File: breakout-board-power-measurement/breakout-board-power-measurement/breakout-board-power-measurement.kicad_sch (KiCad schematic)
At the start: 83 parts, among them J1 Screw_Terminal_01x04, J2 Conn_01x09, J3 Conn_01x07, J4 Conn_01x02, U1 MCP3911A0-E-SS, U2 Si8641BA-B-IU, U3 LM317_TO-252, Y1 10M

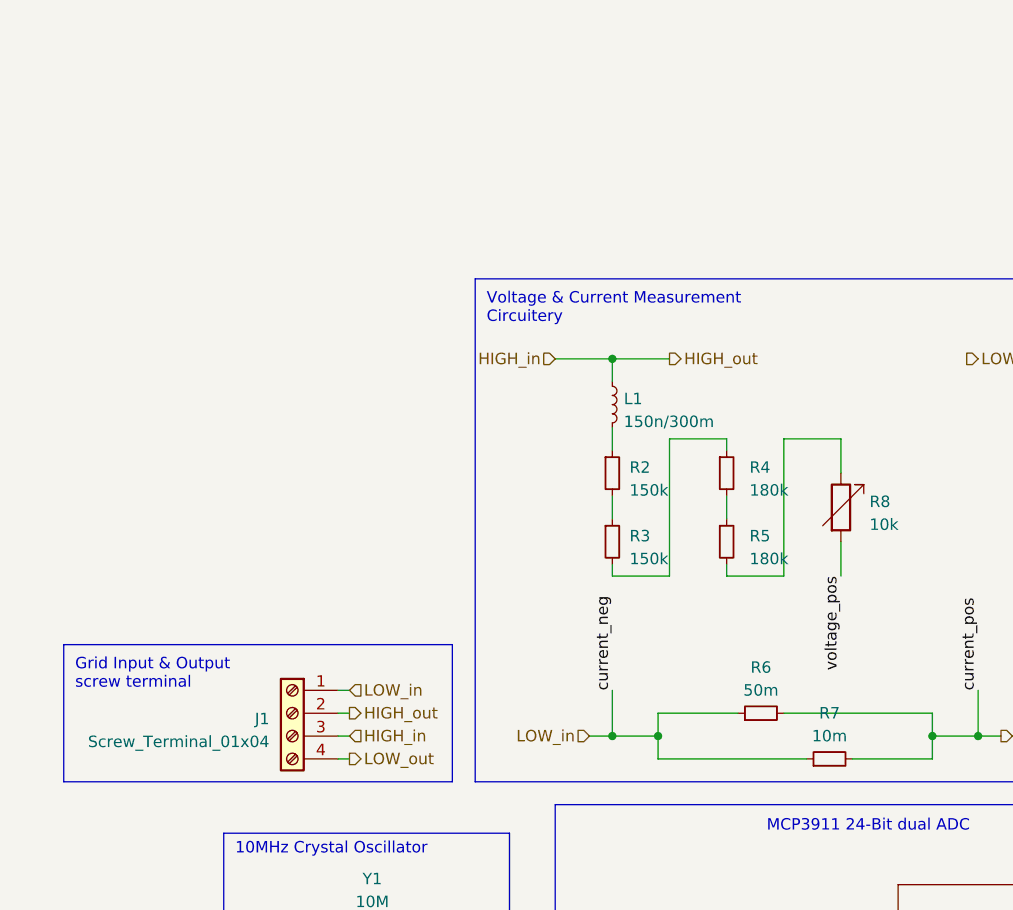
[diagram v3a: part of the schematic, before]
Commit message: Updated PCB layout according to new schematic.(ASM1117-> LM317) (Beidl update)
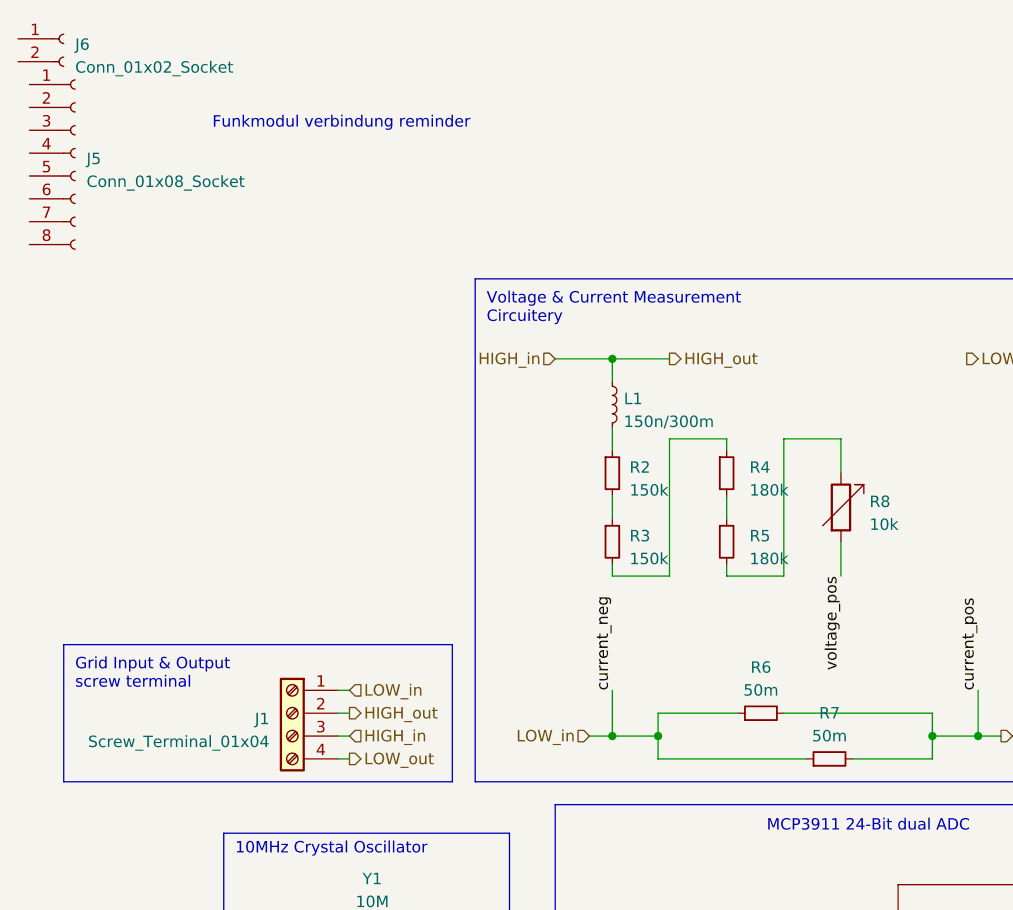
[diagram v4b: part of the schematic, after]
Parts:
- added J5: Conn_01x08_Socket, symbol Connector:Conn_01x08_Socket
- added J6: Conn_01x02_Socket, symbol Connector:Conn_01x02_Socket
- R7: value 10m -> 50m
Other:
- note added: "Funkmodul verbindung reminder"
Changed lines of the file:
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@@
+    (effects (font (size 1.27 1.27)) (justify left bottom))
+  )
+  (text "Funkmodul verbindung reminder\n" (at 44.45 35.56 0)
     (effects (font (size 1.27 1.27)) (justify left bottom))
   )
@@
       (effects (font (size 1.27 1.27)))
     )
-    (property "Value" "10m" (at 113.03 102.87 90)
+    (property "Value" "50m" (at 113.03 102.87 90)
       (effects (font (size 1.27 1.27)))
     )
@@
         (path "/433e477a-c382-4a77-a1aa-b42c4a1fe28b"
           (reference "#PWR011") (unit 1)
+        )
+      )
+    )
+  )
+  (symbol (lib_id "Connector:Conn_01x02_Socket") (at 27.94 25.4 0) (unit 1)
+    (in_bom yes) (on_board yes) (dnp no) (fields_autoplaced)
+    (property "Reference" "J6" (at 29.21 26.035 0)
+      (effects (font (size 1.27 1.27)) (justify left))
+    )
+    (property "Value" "Conn_01x02_Socket" (at 29.21 28.575 0)
+      (effects (font (size 1.27 1.27)) (justify left))
+    )
+    (property "Footprint" "" (at 27.94 25.4 0)
+      (effects (font (size 1.27 1.27)) hide)
+    )
+    (property "Datasheet" "~" (at 27.94 25.4 0)
+      (effects (font (size 1.27 1.27)) hide)
+    )
+    (pin "1")
+    (pin "2")
+    (instances
+      (project "breakout-board-power-measurement"
+        (path "/433e477a-c382-4a77-a1aa-b42c4a1fe28b"
+          (reference "J6") (unit 1)
         )
       )
@@
         )
       )
+    )
+  )
+  (symbol (lib_id "Connector:Conn_01x08_Socket") (at 29.21 38.1 0) (unit 1)
+    (in_bom yes) (on_board yes) (dnp no) (fields_autoplaced)
+    (property "Reference" "J5" (at 30.48 38.735 0)
+      (effects (font (size 1.27 1.27)) (justify left))
+    )
+    (property "Value" "Conn_01x08_Socket" (at 30.48 41.275 0)
+      (effects (font (size 1.27 1.27)) (justify left))
+    )
+    (property "Footprint" "" (at 29.21 38.1 0)
+      (effects (font (size 1.27 1.27)) hide)
+    )
+    (property "Datasheet" "~" (at 29.21 38.1 0)
+      (effects (font (size 1.27 1.27)) hide)
+    )
+    (pin "1")
+    (pin "2")
+    (pin "3")
+    (pin "4")
+    (pin "5")
+    (pin "6")
+    (pin "7")
+    (pin "8")
+    (instances
+      (project "breakout-board-power-measurement"
+        (path "/433e477a-c382-4a77-a1aa-b42c4a1fe28b"
+          (reference "J5") (unit 1)
+        )
+      )

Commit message: Fixed SPI
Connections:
- net SDI: now also R21.1, U1.20 (SDI); no longer R17.1, U1.19 (SDO)
- net SDI_: now also J2.2 (Pin_2), R21.2, TP16.1, U2.12 (B3); no longer J2.3 (Pin_3), R17.2, TP17.1
- net SDO: now also R17.1, U1.19 (SDO); no longer R21.1, U1.20 (SDI)
- net SDO_: now also J2.3 (Pin_3), R17.2, TP17.1; no longer J2.2 (Pin_2), R21.2, TP16.1
- net ~{RESET}_: no longer U2.12 (B3)
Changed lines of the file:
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@@
   (junction (at 267.97 140.97) (diameter 0) (color 0 0 0 0)
   )
+  (junction (at 237.49 184.15) (diameter 0) (color 0 0 0 0)
+  )
   (junction (at 269.24 161.29) (diameter 0) (color 0 0 0 0)
   )
   (junction (at 177.165 86.36) (diameter 0) (color 0 0 0 0)
   )
-  (junction (at 237.49 181.61) (diameter 0) (color 0 0 0 0)
-  )
   (junction (at 177.165 71.12) (diameter 0) (color 0 0 0 0)
   )
@@
   (junction (at 261.62 120.65) (diameter 0) (color 0 0 0 0)
   )
-  (junction (at 234.95 184.15) (diameter 0) (color 0 0 0 0)
-  )
   (junction (at 129.54 102.87) (diameter 0) (color 0 0 0 0)
   )
@@
   )
   (junction (at 232.41 161.29) (diameter 0) (color 0 0 0 0)
+  )
+  (junction (at 234.95 186.69) (diameter 0) (color 0 0 0 0)
   )
   (no_connect (at 339.09 151.13))
@@
     (stroke (width 0) (type default))
   )
-  (wire (pts (xy 219.71 181.61) (xy 237.49 181.61))
+  (wire (pts (xy 219.71 181.61) (xy 250.19 181.61))
     (stroke (width 0) (type default))
   )
@@
     (stroke (width 0) (type default))
   )
-  (wire (pts (xy 237.49 153.67) (xy 237.49 181.61))
-    (stroke (width 0) (type default))
-  )
   (wire (pts (xy 337.82 64.77) (xy 339.09 64.77))
     (stroke (width 0) (type default))
@@
     (stroke (width 0) (type default))
   )
-  (wire (pts (xy 237.49 181.61) (xy 250.19 181.61))
-    (stroke (width 0) (type default))
-  )
   (wire (pts (xy 265.43 148.59) (xy 270.51 148.59))
     (stroke (width 0) (type default))
@@
     (stroke (width 0) (type default))
   )
+  (wire (pts (xy 237.49 184.15) (xy 250.19 184.15))
+    (stroke (width 0) (type default))
+  )
   (wire (pts (xy 164.465 64.77) (xy 164.465 63.5))
     (stroke (width 0) (type default))
@@
     (stroke (width 0) (type default))
   )
-  (wire (pts (xy 234.95 156.21) (xy 234.95 184.15))
-    (stroke (width 0) (type default))
-  )
   (wire (pts (xy 237.49 104.14) (xy 237.49 109.22))
     (stroke (width 0) (type default))
@@
     (stroke (width 0) (type default))
   )
+  (wire (pts (xy 234.95 186.69) (xy 250.19 186.69))
+    (stroke (width 0) (type default))
+  )
   (wire (pts (xy 280.035 104.14) (xy 287.02 104.14))
     (stroke (width 0) (type default))
@@
     (stroke (width 0) (type default))
   )
+  (wire (pts (xy 234.95 156.21) (xy 234.95 186.69))
+    (stroke (width 0) (type default))
+  )
   (polyline (pts (xy 201.93 90.17) (xy 209.55 90.17))
     (stroke (width 0) (type default))
@@
     (stroke (width 0) (type default))
   )
-  (wire (pts (xy 234.95 184.15) (xy 250.19 184.15))
-    (stroke (width 0) (type default))
-  )
   (wire (pts (xy 212.09 194.31) (xy 214.63 194.31))
     (stroke (width 0) (type default))
@@
     (stroke (width 0) (type default))
   )
-  (wire (pts (xy 226.06 186.69) (xy 250.19 186.69))
+  (wire (pts (xy 226.06 186.69) (xy 234.95 186.69))
     (stroke (width 0) (type default))
   )
@@
     (stroke (width 0) (type default))
   )
-  (wire (pts (xy 232.41 184.15) (xy 234.95 184.15))
+  (wire (pts (xy 232.41 184.15) (xy 237.49 184.15))
     (stroke (width 0) (type default))
   )
@@
   )
   (wire (pts (xy 177.165 78.74) (xy 189.865 78.74))
+    (stroke (width 0) (type default))
+  )
+  (wire (pts (xy 237.49 153.67) (xy 237.49 184.15))
     (stroke (width 0) (type default))
   )
@@
     (effects (font (size 1.27 1.27)) (justify right bottom))
   )
-  (label "SDI_" (at 248.92 186.69 180) (fields_autoplaced)
+  (label "SDI_" (at 248.92 184.15 180) (fields_autoplaced)
     (effects (font (size 1.27 1.27)) (justify right bottom))
   )
@@
     (effects (font (size 1.27 1.27)) (justify right bottom))
   )
-  (label "SDO_" (at 248.92 184.15 180) (fields_autoplaced)
+  (label "SDO_" (at 248.92 186.69 180) (fields_autoplaced)
     (effects (font (size 1.27 1.27)) (justify right bottom))
   )
@@
     (effects (font (size 1.27 1.27)) (justify right bottom))
   )
-  (label "SDI_" (at 339.09 120.65 180) (fields_autoplaced)
+  (label "SDI_" (at 339.09 116.205 180) (fields_autoplaced)
     (effects (font (size 1.27 1.27)) (justify right bottom))
   )
@@
     (effects (font (size 1.27 1.27)) (justify right bottom))
   )
-  (label "SDI" (at 110.49 157.48 180) (fields_autoplaced)
+  (label "SDI" (at 110.49 154.94 180) (fields_autoplaced)
     (effects (font (size 1.27 1.27)) (justify right bottom))
   )
@@
     (effects (font (size 1.27 1.27)) (justify right bottom))
   )
-  (label "SDO" (at 212.09 184.15 180) (fields_autoplaced)
+  (label "SDO" (at 212.09 186.69 180) (fields_autoplaced)
     (effects (font (size 1.27 1.27)) (justify right bottom))
   )
@@
     (effects (font (size 1.27 1.27)) (justify right bottom))
   )
-  (label "SDO" (at 110.49 154.94 180) (fields_autoplaced)
-    (effects (font (size 1.27 1.27)) (justify right bottom))
-  )
-  (label "SDO_" (at 339.09 116.205 180) (fields_autoplaced)
+  (label "SDO" (at 110.49 157.48 180) (fields_autoplaced)
+    (effects (font (size 1.27 1.27)) (justify right bottom))
+  )
+  (label "SDO_" (at 339.09 120.65 180) (fields_autoplaced)
     (effects (font (size 1.27 1.27)) (justify right bottom))
   )
@@
     (effects (font (size 1.27 1.27)) (justify left bottom))
   )
-  (label "SDI" (at 212.09 186.69 180) (fields_autoplaced)
-    (effects (font (size 1.27 1.27)) (justify right bottom))
-  )
+  (label "SDI" (at 212.09 184.15 180) (fields_autoplaced)
+    (effects (font (size 1.27 1.27)) (justify right bottom))
+  )

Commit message: Important fixes SDI/SDO swap, reset
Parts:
- removed J5: Conn_01x08_Socket, symbol Connector:Conn_01x08_Socket
- removed J6: Conn_01x02_Socket, symbol Connector:Conn_01x02_Socket
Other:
- note removed: "Funkmodul verbindung reminder"

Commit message: Power measurement final almst ready
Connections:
- net CH0+: now also C6.2, R13.2; no longer C4.2, R10.2
- net CH0-: now also C5.1, R12.2; no longer C3.1, R11.2
- net CH1+: now also C3.1, R11.2, U1.7 (CH1+); no longer C5.1, R12.2, U1.6 (CH1-)
- net CH1-: now also C4.2, R10.2, U1.6 (CH1-); no longer C6.2, R13.2, U1.7 (CH1+)
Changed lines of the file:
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@@
     (stroke (width 0) (type default))
   )
-  (wire (pts (xy 189.865 69.85) (xy 192.405 69.85))
+  (wire (pts (xy 189.865 69.85) (xy 193.04 69.85))
     (stroke (width 0) (type default))
   )
@@
     (stroke (width 0) (type default))
   )
-  (wire (pts (xy 189.865 72.39) (xy 192.405 72.39))
+  (wire (pts (xy 189.865 72.39) (xy 193.04 72.39))
     (stroke (width 0) (type default))
   )
@@
     (stroke (width 0) (type default))
   )
-  (wire (pts (xy 189.865 92.71) (xy 192.405 92.71))
+  (wire (pts (xy 189.865 92.71) (xy 193.04 92.71))
     (stroke (width 0) (type default))
   )
@@
     (stroke (width 0) (type default))
   )
-  (wire (pts (xy 189.865 95.25) (xy 192.405 95.25))
+  (wire (pts (xy 189.865 95.25) (xy 193.04 95.25))
     (stroke (width 0) (type default))
   )
@@
     (effects (font (size 1.27 1.27)) (justify right bottom))
   )
-  (label "CH1-" (at 192.405 95.25 0) (fields_autoplaced)
+  (label "CH1-" (at 193.04 72.39 0) (fields_autoplaced)
     (effects (font (size 1.27 1.27)) (justify left bottom))
   )
@@
     (effects (font (size 1.27 1.27)) (justify right bottom))
   )
-  (label "CH1+" (at 192.405 92.71 0) (fields_autoplaced)
+  (label "CH1+" (at 193.04 69.85 0) (fields_autoplaced)
     (effects (font (size 1.27 1.27)) (justify left bottom))
   )
@@
     (effects (font (size 1.27 1.27)) (justify right bottom))
   )
-  (label "CH1-" (at 110.49 137.16 180) (fields_autoplaced)
+  (label "CH1-" (at 110.49 134.62 180) (fields_autoplaced)
     (effects (font (size 1.27 1.27)) (justify right bottom))
   )
@@
     (effects (font (size 1.27 1.27)) (justify right bottom))
   )
-  (label "CH1+" (at 110.49 134.62 180) (fields_autoplaced)
+  (label "CH1+" (at 110.49 137.16 180) (fields_autoplaced)
     (effects (font (size 1.27 1.27)) (justify right bottom))
   )
@@
     (effects (font (size 1.27 1.27)) (justify right bottom))
   )
-  (label "CH0+" (at 192.405 72.39 0) (fields_autoplaced)
+  (label "CH0+" (at 193.04 95.25 0) (fields_autoplaced)
     (effects (font (size 1.27 1.27)) (justify left bottom))
   )
@@
     (effects (font (size 1.27 1.27)) (justify left bottom))
   )
-  (label "CH0-" (at 192.405 69.85 0) (fields_autoplaced)
-    (effects (font (size 1.27 1.27)) (justify left bottom))
-  )
+  (label "CH0-" (at 193.04 92.71 0) (fields_autoplaced)
+    (effects (font (size 1.27 1.27)) (justify left bottom))
+  )
